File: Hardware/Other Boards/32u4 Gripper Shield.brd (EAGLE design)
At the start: 31.8 x 55.9 mm, 16 parts, among them U1 SN74LS241DW, U2 XBEE-1B3

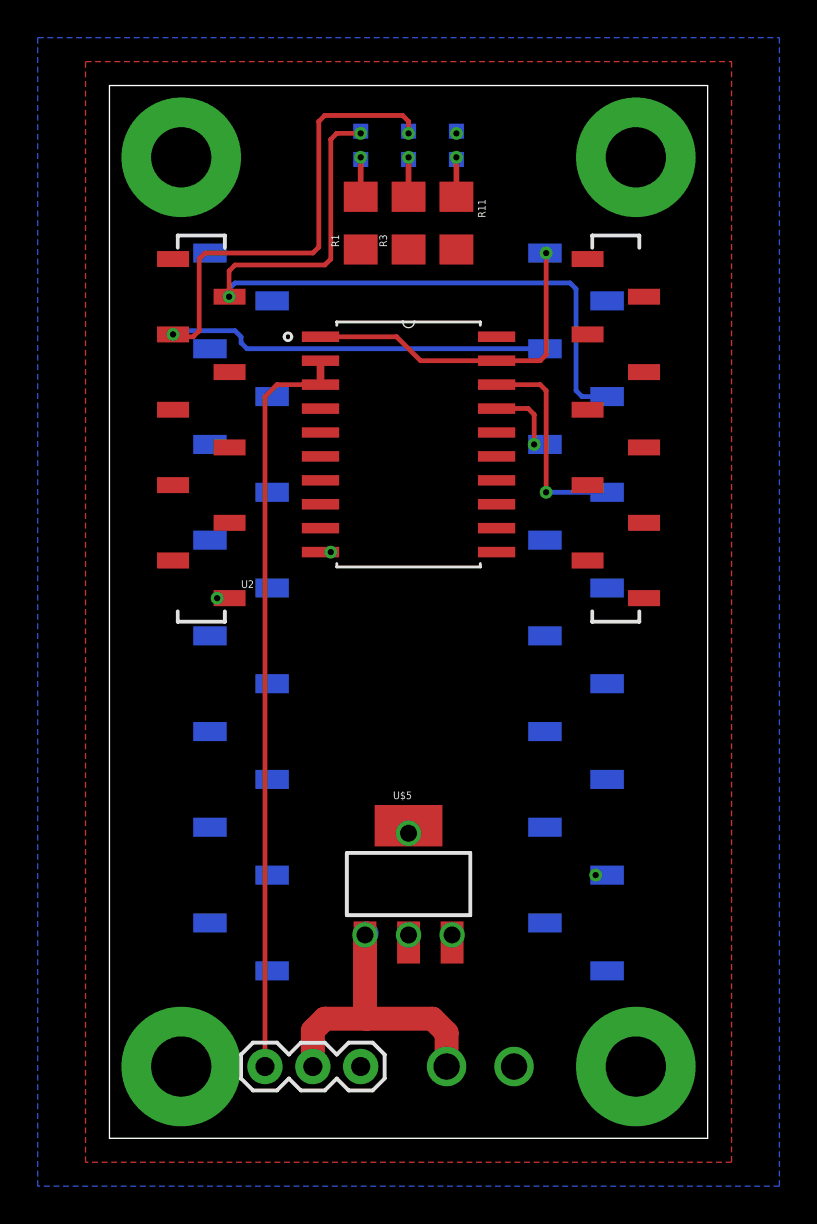
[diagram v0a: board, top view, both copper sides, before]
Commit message: Finished shields for aux
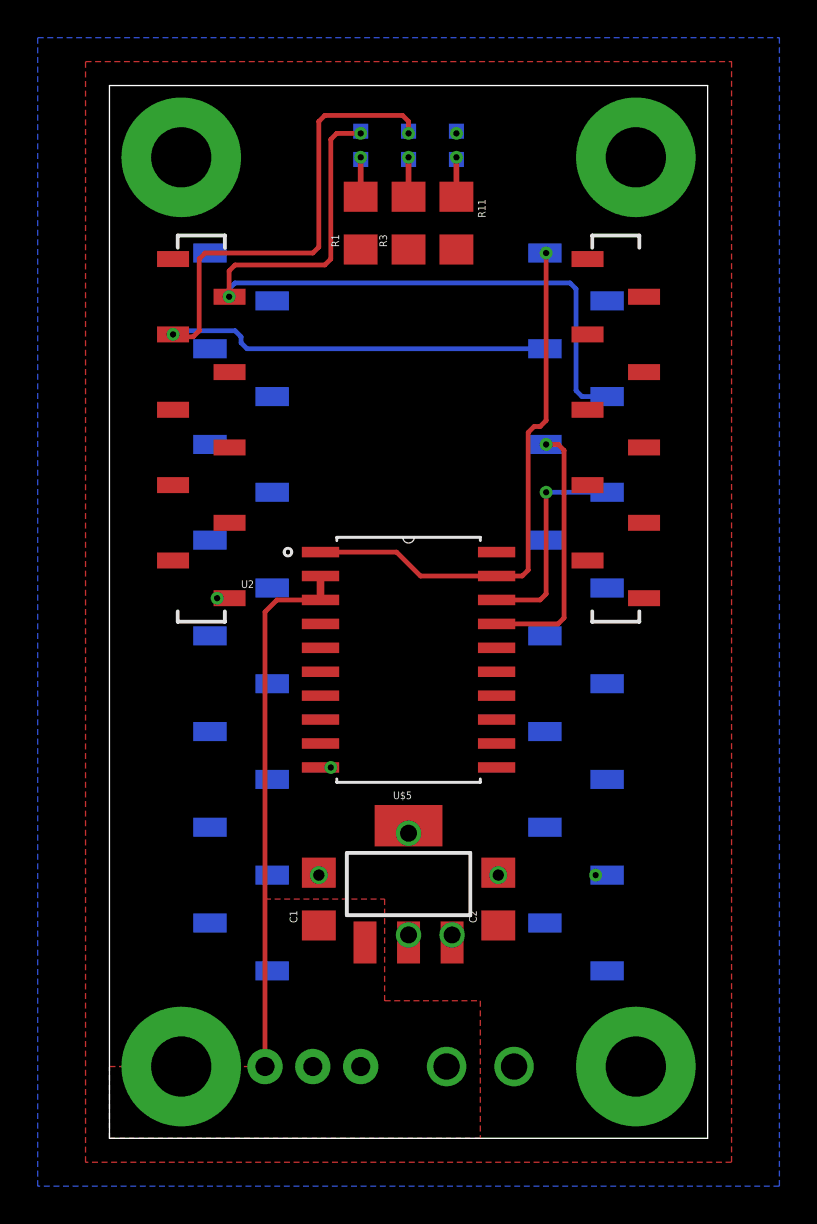
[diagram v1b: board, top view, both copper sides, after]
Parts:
- added C1, C2: (no value), SparkFun-Passives:1206
- moved U1 11.4 mm to (15.9, 25.4)
- flipped JP1 to the bottom, turned to 180 degrees
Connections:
- net 12V: now also C1.1
- net 3.3V: now also C2.1
- net GND: now also C1.2, C2.2
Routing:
- net 12V: track 16.0 -> 0.00 mm, vias 1 -> 0
- net DDATA_1: track 40.0 -> 28.6 mm
- net DC_1: track 18.2 -> 29.2 mm
- net TX_1: track 4.28 -> 13.8 mm
- net GND: track 3.47 -> 3.73 mm, vias 5 -> 7
- added copper zone on layer 1, net 12V
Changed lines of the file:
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@@
 </autorouter>
 <elements>
-<element name="JP1" library="SparkFun-Connectors" package="1X03" value="" x="8.255" y="3.81" smashed="yes">
-<attribute name="VALUE" x="6.985" y="0.635" size="1.27" layer="27"/>
+<element name="JP1" library="SparkFun-Connectors" package="1X03" value="" x="8.255" y="3.81" smashed="yes" rot="MR180">
+<attribute name="VALUE" x="6.985" y="6.985" size="1.27" layer="28" rot="MR180"/>
 </element>
 <element name="LED1" library="SparkFun" package="LED-0603" value="Red" x="18.415" y="52.705" rot="MR0"/>
@@
 </element>
 <element name="U$5" library="SparkFun-PowerIC" package="SOT223" value="V_REG_MIC2920" x="15.875" y="13.49375"/>
-<element name="U1" library="74LS241" package="SOIC127P1030X265-20N" value="SN74LS241DW" x="15.875" y="36.83" smashed="yes">
-<attribute name="PACKAGE" value="SOIC-20" x="15.875" y="36.83" size="1.778" layer="27" display="off"/>
-<attribute name="OC_NEWARK" value="50R6539 " x="15.875" y="36.83" size="1.778" layer="27" display="off"/>
-<attribute name="MPN" value="SN74LS241DW" x="15.875" y="36.83" size="1.778" layer="27" display="off"/>
-<attribute name="SUPPLIER" value="Texas Instruments" x="15.875" y="36.83" size="1.778" layer="27" display="off"/>
-<attribute name="OC_FARNELL" value="1739687" x="15.875" y="36.83" size="1.778" layer="27" display="off"/>
+<element name="U1" library="74LS241" package="SOIC127P1030X265-20N" value="SN74LS241DW" x="15.875" y="25.4" smashed="yes">
+<attribute name="PACKAGE" value="SOIC-20" x="15.875" y="25.4" size="1.778" layer="27" display="off"/>
+<attribute name="OC_NEWARK" value="50R6539 " x="15.875" y="25.4" size="1.778" layer="27" display="off"/>
+<attribute name="MPN" value="SN74LS241DW" x="15.875" y="25.4" size="1.778" layer="27" display="off"/>
+<attribute name="SUPPLIER" value="Texas Instruments" x="15.875" y="25.4" size="1.778" layer="27" display="off"/>
+<attribute name="OC_FARNELL" value="1739687" x="15.875" y="25.4" size="1.778" layer="27" display="off"/>
 </element>
 <element name="U2" library="SparkFun" package="XBEE-SMD" value="XBEE-1B3" x="15.875" y="26.67"/>
@@
 <element name="S3" library="SparkFun-Electromechanical" package="STANDOFF-ELECTRICAL" value="STANDOFF_ELECTRICAL" x="3.81" y="3.81"/>
 <element name="S4" library="SparkFun-Electromechanical" package="STANDOFF-ELECTRICAL" value="STANDOFF_ELECTRICAL" x="27.94" y="3.81"/>
+<element name="C1" library="SparkFun-Passives" package="1206" value="" x="11.1125" y="12.7" rot="R90"/>
+<element name="C2" library="SparkFun-Passives" package="1206" value="" x="20.6375" y="12.7" rot="R90"/>
 </elements>
 <signals>
@@
 <via x="5.715" y="28.67" extent="1-16" drill="0.3302"/>
 <wire x1="6.375" y1="28.67" x2="5.715" y2="28.67" width="0.4064" layer="1"/>
-<via x="11.7475" y="31.115" extent="1-16" drill="0.3302"/>
-<wire x1="11.2014" y1="31.115" x2="11.7475" y2="31.115" width="0.4064" layer="1"/>
+<via x="11.7475" y="19.685" extent="1-16" drill="0.3302"/>
+<wire x1="11.2014" y1="19.685" x2="11.7475" y2="19.685" width="0.4064" layer="1"/>
 <contactref element="S1" pad="P1"/>
 <contactref element="S2" pad="P1"/>
@@
 <wire x1="15.875" y1="10.39495" x2="15.875" y2="10.795" width="0.4064" layer="1"/>
 <wire x1="15.875" y1="16.59275" x2="15.875" y2="16.1925" width="0.4064" layer="1"/>
+<contactref element="C1" pad="2"/>
+<contactref element="C2" pad="2"/>
+<via x="11.1125" y="13.97" extent="1-16" drill="0.6" shape="square"/>
+<via x="20.6375" y="13.97" extent="1-16" drill="0.6" shape="square"/>
+<wire x1="11.1125" y1="14.1" x2="11.1125" y2="13.97" width="0.4064" layer="1"/>
+<wire x1="20.6375" y1="14.1" x2="20.6375" y2="13.97" width="0.4064" layer="1"/>
 </signal>
 <signal name="RESET">
@@
 <contactref element="U1" pad="20"/>
 <contactref element="U$5" pad="3"/>
-<polygon width="0.3048" layer="1" isolate="0.1524">
+<polygon width="0.3048" layer="1" isolate="0.1524" rank="2">
 <vertex x="-1.27" y="-1.27"/>
 <vertex x="-1.27" y="57.15"/>
@@
 <via x="25.8064" y="13.97" extent="1-16" drill="0.3302"/>
 <wire x1="25.8064" y1="13.97" x2="26.416" y2="13.97" width="0.3048" layer="16"/>
+<contactref element="C2" pad="1"/>
 </signal>
 <signal name="DIO4">
@@
 <contactref element="U1" pad="19"/>
 <contactref element="U$1" pad="P$16"/>
-<wire x1="20.5486" y1="41.275" x2="22.86" y2="41.275" width="0.254" layer="1"/>
-<wire x1="22.86" y1="41.275" x2="23.1775" y2="41.5925" width="0.254" layer="1"/>
-<wire x1="23.1775" y1="41.5925" x2="23.1775" y2="46.99" width="0.254" layer="1"/>
 <via x="23.1775" y="46.99" extent="1-16" drill="0.3302"/>
 <wire x1="23.1775" y1="46.99" x2="23.1775" y2="46.9265" width="0.254" layer="16"/>
 <wire x1="23.1775" y1="46.9265" x2="23.114" y2="46.99" width="0.254" layer="16"/>
-<wire x1="11.2014" y1="42.545" x2="15.24" y2="42.545" width="0.254" layer="1"/>
-<wire x1="15.24" y1="42.545" x2="16.51" y2="41.275" width="0.254" layer="1"/>
-<wire x1="16.51" y1="41.275" x2="20.5486" y2="41.275" width="0.254" layer="1"/>
+<wire x1="11.2014" y1="31.115" x2="15.24" y2="31.115" width="0.254" layer="1"/>
+<wire x1="15.24" y1="31.115" x2="16.51" y2="29.845" width="0.254" layer="1"/>
+<wire x1="16.51" y1="29.845" x2="20.5486" y2="29.845" width="0.254" layer="1"/>
+<wire x1="23.1775" y1="46.99" x2="23.1775" y2="38.1" width="0.254" layer="1"/>
+<wire x1="23.1775" y1="38.1" x2="22.86" y2="37.7825" width="0.254" layer="1"/>
+<wire x1="22.86" y1="37.7825" x2="22.5425" y2="37.7825" width="0.254" layer="1"/>
+<wire x1="22.5425" y1="37.7825" x2="22.225" y2="37.465" width="0.254" layer="1"/>
+<wire x1="22.225" y1="37.465" x2="22.225" y2="30.1625" width="0.254" layer="1"/>
+<wire x1="22.225" y1="30.1625" x2="21.9075" y2="29.845" width="0.254" layer="1"/>
+<wire x1="21.9075" y1="29.845" x2="20.5486" y2="29.845" width="0.254" layer="1"/>
 </signal>
 <signal name="DDATA_1">
@@
 <contactref element="U1" pad="3"/>
 <contactref element="JP1" pad="1"/>
-<wire x1="11.2014" y1="41.275" x2="11.2014" y2="40.005" width="0.4064" layer="1"/>
-<wire x1="8.255" y1="3.81" x2="8.255" y2="39.37" width="0.254" layer="1"/>
-<wire x1="8.255" y1="39.37" x2="8.89" y2="40.005" width="0.254" layer="1"/>
-<wire x1="8.89" y1="40.005" x2="11.2014" y2="40.005" width="0.254" layer="1"/>
+<wire x1="11.2014" y1="29.845" x2="11.2014" y2="28.575" width="0.4064" layer="1"/>
+<wire x1="8.255" y1="27.94" x2="8.89" y2="28.575" width="0.254" layer="1"/>
+<wire x1="8.89" y1="28.575" x2="11.2014" y2="28.575" width="0.254" layer="1"/>
+<wire x1="8.255" y1="27.94" x2="8.255" y2="3.81" width="0.254" layer="1"/>
 </signal>
 <signal name="RX_1">
@@
 <wire x1="26.416" y1="34.29" x2="23.1775" y2="34.29" width="0.254" layer="16"/>
 <via x="23.1775" y="34.29" extent="1-16" drill="0.3302"/>
-<wire x1="23.1775" y1="34.29" x2="23.1775" y2="39.6875" width="0.254" layer="1"/>
-<wire x1="23.1775" y1="39.6875" x2="22.86" y2="40.005" width="0.254" layer="1"/>
-<wire x1="22.86" y1="40.005" x2="20.5486" y2="40.005" width="0.254" layer="1"/>
+<wire x1="23.1775" y1="34.29" x2="23.1775" y2="28.8925" width="0.254" layer="1"/>
+<wire x1="23.1775" y1="28.8925" x2="22.86" y2="28.575" width="0.254" layer="1"/>
+<wire x1="22.86" y1="28.575" x2="20.5486" y2="28.575" width="0.254" layer="1"/>
 </signal>
 <signal name="TX_1">
 <contactref element="U1" pad="17"/>
 <contactref element="U$1" pad="P$12"/>
-<wire x1="23.114" y1="36.83" x2="22.5425" y2="36.83" width="0.254" layer="16"/>
-<via x="22.5425" y="36.83" extent="1-16" drill="0.3302"/>
-<wire x1="22.225" y1="38.735" x2="20.5486" y2="38.735" width="0.254" layer="1"/>
-<wire x1="22.5425" y1="36.83" x2="22.5425" y2="38.4175" width="0.254" layer="1"/>
-<wire x1="22.5425" y1="38.4175" x2="22.225" y2="38.735" width="0.254" layer="1"/>
+<wire x1="23.114" y1="36.83" x2="23.1775" y2="36.83" width="0.254" layer="16"/>
+<via x="23.1775" y="36.83" extent="1-16" drill="0.3302"/>
+<wire x1="23.1775" y1="36.83" x2="23.8125" y2="36.83" width="0.254" layer="1"/>
+<wire x1="23.8125" y1="36.83" x2="24.13" y2="36.5125" width="0.254" layer="1"/>
+<wire x1="24.13" y1="36.5125" x2="24.13" y2="27.6225" width="0.254" layer="1"/>
+<wire x1="24.13" y1="27.6225" x2="23.8125" y2="27.305" width="0.254" layer="1"/>
+<wire x1="23.8125" y1="27.305" x2="20.5486" y2="27.305" width="0.254" layer="1"/>
 </signal>
 <signal name="12V">
@@
 <contactref element="U$5" pad="1"/>
 <contactref element="U$3" pad="L"/>
-<via x="13.5636" y="10.795" extent="1-16" drill="0.9" shape="square"/>
-<wire x1="13.5636" y1="10.795" x2="13.5636" y2="10.39495" width="0.4064" layer="1"/>
-<wire x1="13.6525" y1="10.8839" x2="13.5636" y2="10.795" width="1.27" layer="16"/>
-<wire x1="17.895" y1="3.81" x2="17.895" y2="5.6" width="1.27" layer="1"/>
-<wire x1="17.895" y1="5.6" x2="17.145" y2="6.35" width="1.27" layer="1"/>
-<wire x1="17.145" y1="6.35" x2="13.6525" y2="6.35" width="1.27" layer="1"/>
-<wire x1="13.6525" y1="6.35" x2="11.43" y2="6.35" width="1.27" layer="1"/>
-<wire x1="11.43" y1="6.35" x2="10.795" y2="5.715" width="1.27" layer="1"/>
-<wire x1="10.795" y1="5.715" x2="10.795" y2="3.81" width="1.27" layer="1"/>
-<wire x1="13.5636" y1="10.39495" x2="13.5636" y2="6.4389" width="1.27" layer="1"/>
-<wire x1="13.5636" y1="6.4389" x2="13.6525" y2="6.35" width="1.27" layer="1"/>
+<contactref element="C1" pad="1"/>
+<polygon width="0.3048" layer="1" isolate="0.1524" thermals="no">
+<vertex x="0" y="0"/>
+<vertex x="0" y="3.81"/>
+<vertex x="8.255" y="3.81"/>
+<vertex x="8.255" y="12.7"/>
+<vertex x="14.605" y="12.7"/>
+<vertex x="14.605" y="7.3025"/>
+<vertex x="19.685" y="7.3025"/>
+<vertex x="19.685" y="0"/>
+</polygon>
 </signal>
 <signal name="TX_0">
